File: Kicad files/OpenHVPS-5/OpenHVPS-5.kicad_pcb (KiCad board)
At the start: 2 copper layers, 40.6 x 20.8 mm, 80 parts, among them J1 Conn_01x03_Male, Q1 FQT7N10, Q2 BC846A, Q3 MMDT3906, U1 MAX6008AEUR+T, U2 74HC14, U3 MAX4162, U4 CD14538BM

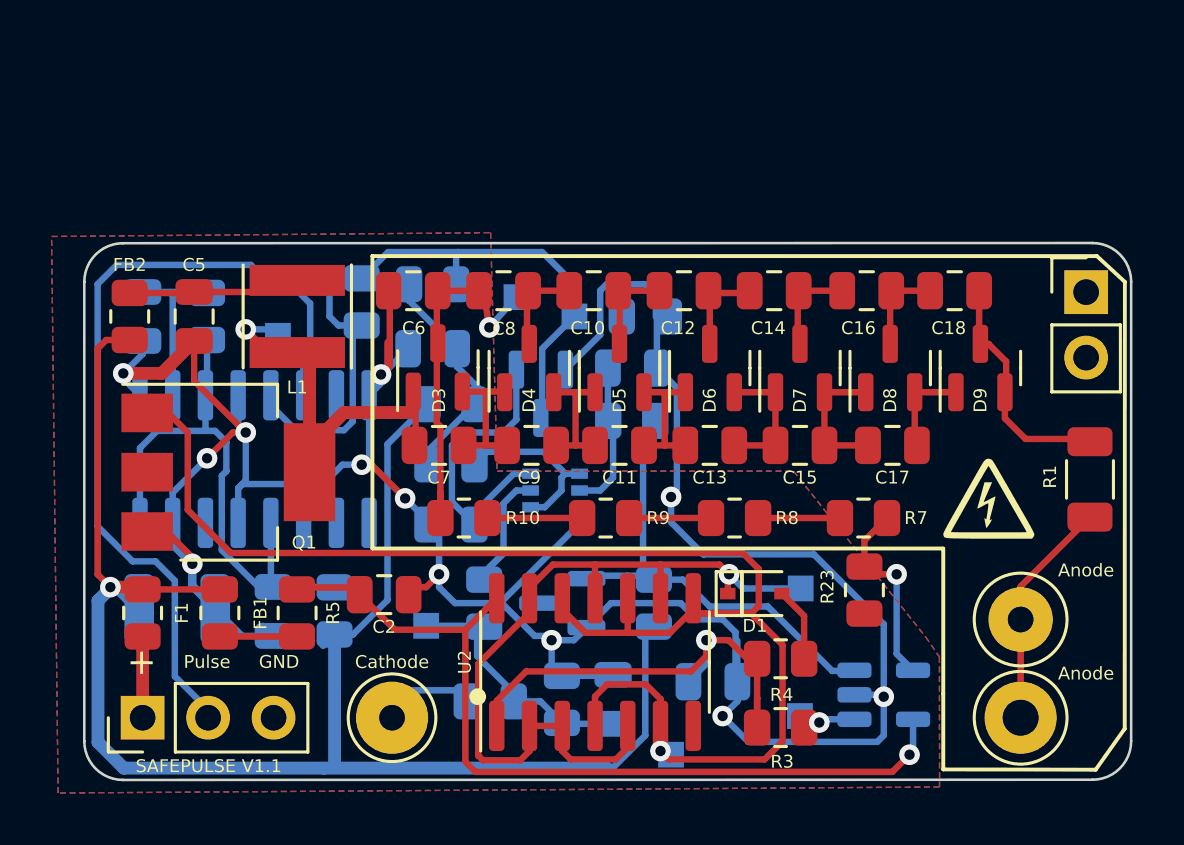
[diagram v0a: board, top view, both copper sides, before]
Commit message: Changed Q3 package to single transitor. Now Q3+Q4
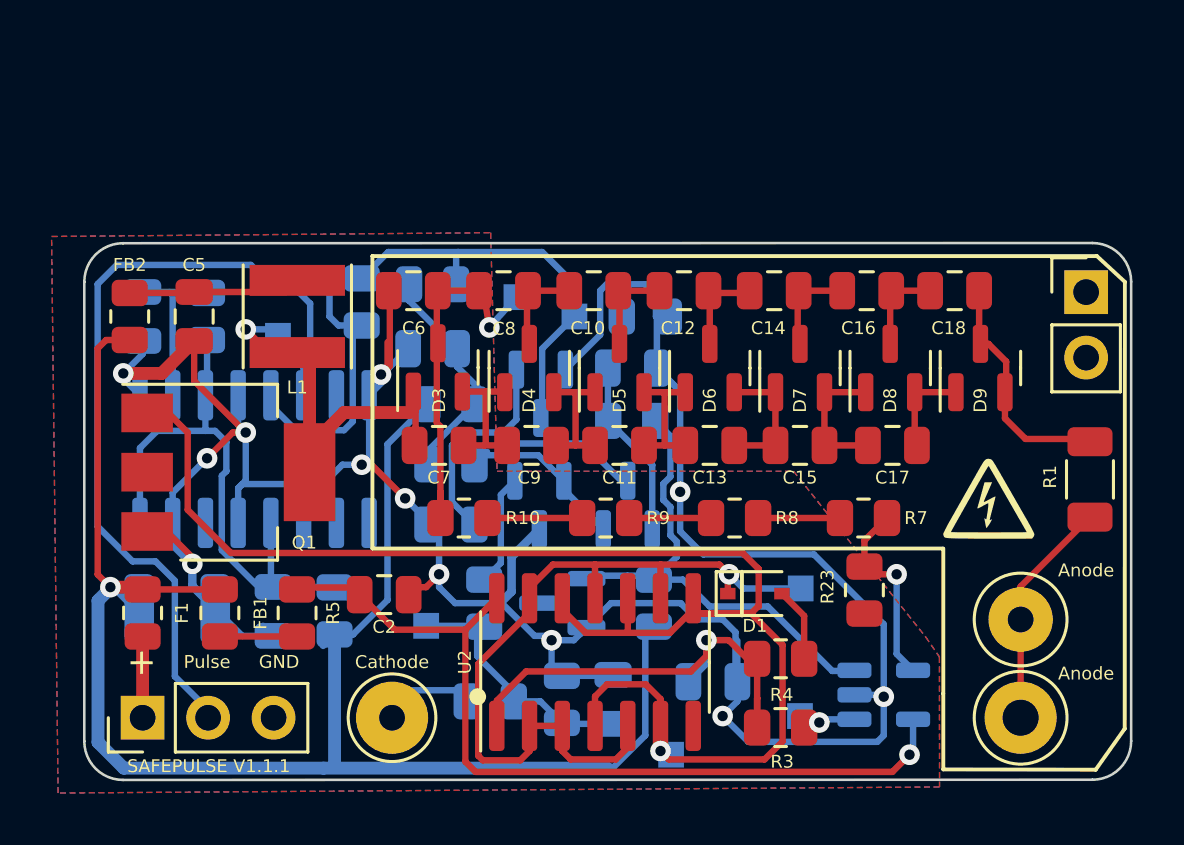
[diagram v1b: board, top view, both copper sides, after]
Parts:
- removed TP1: TestPoint, TestPoint:TestPoint_Pad_1.0x1.0mm
- added Q4: MMBT3906, Package_TO_SOT_SMD:SOT-23, B.Cu at (143.9, 67.3)
- Q3: value MMDT3906 -> MMBT3906; footprint Package_TO_SOT_SMD:SOT-363_SC-70-6 -> Package_TO_SOT_SMD:SOT-23
- moved Q3 2.88 mm to (147.3, 67.3), turned to 90 degrees
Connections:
- Q3 pad 1: Net-(Q3-Pad1) -> Net-(C24-Pad1)
- Q3 pad 2: Net-(C24-Pad1) -> Net-(R17-Pad2)
- Q3 pad 3: GND -> Net-(Q2-Pad1)
- R17 pad 2: Net-(Q3-Pad1) -> Net-(R17-Pad2)
- R19 pad 1: Net-(Q3-Pad5) -> Net-(R19-Pad1)
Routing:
- net Net-(R17-Pad2): track 0.00 -> 7.22 mm
- net Net-(Q3-Pad1): track 6.81 -> 0.00 mm
- net Net-(Q3-Pad5): track 5.39 -> 0.00 mm
- net Net-(R19-Pad1): track 0.00 -> 4.33 mm
- net Net-(Q2-Pad1): track 12.4 -> 15.0 mm
- net +2V5: track 18.9 -> 20.3 mm
- net Net-(C24-Pad1): track 8.12 -> 9.50 mm
- net GND: track 126.5 -> 125.9 mm
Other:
- board text added: "SAFEPULSE V1.1.1"
- board text removed: "SAFEPULSE V1.1"

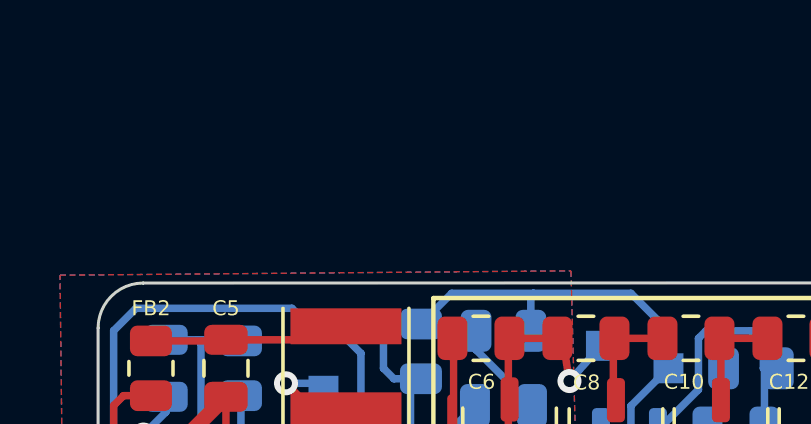
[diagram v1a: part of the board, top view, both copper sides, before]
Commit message: Removed TP1
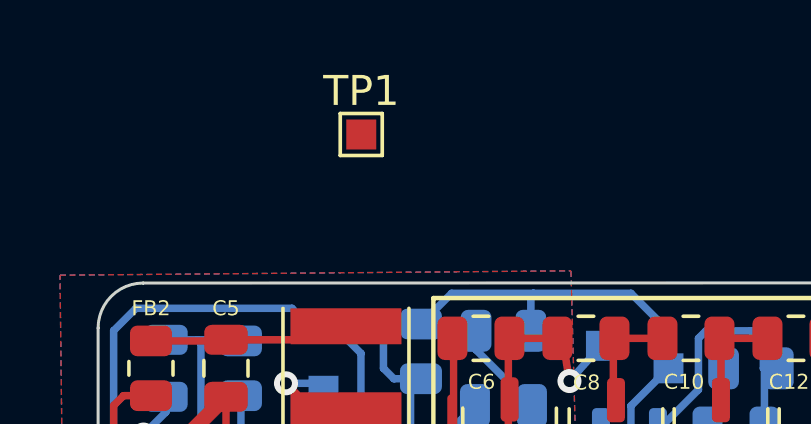
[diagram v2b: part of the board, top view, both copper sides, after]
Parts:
- added TP1: TestPoint, TestPoint:TestPoint_Pad_1.0x1.0mm, F.Cu at (135.0, 52.2)
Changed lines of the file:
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@@
   (net 47 "unconnected-(two_pinheader1-Pad2)")
   (net 48 "unconnected-(two_pinheader1-Pad1)")
-  (net 49 "Net-(R17-Pad2)")
-  (net 50 "Net-(R19-Pad1)")
+  (net 49 "Net-(Q3-Pad2)")
+  (net 50 "Net-(Q4-Pad1)")
   (footprint "Resistor_SMD:R_0805_2012Metric" (layer "F.Cu")
     (at 128.5 71.501 90)
@@
     )
   )
+  (footprint "TestPoint:TestPoint_Pad_1.0x1.0mm" (layer "F.Cu")
+    (at 135.01 52.206)
+    (descr "SMD rectangular pad as test Point, square 1.0mm side length")
+    (tags "test point SMD pad rectangle square")
+    (property "Sheetfile" "OpenHVPS-5.kicad_sch")
+    (property "Sheetname" "")
+    (property "exclude_from_bom" "")
+    (attr exclude_from_pos_files exclude_from_bom)
+    (fp_text reference "TP1" (at 0 -1.448) (layer "F.SilkS")
+      (effects (font (size 1 1) (thickness 0.15)))
+    )
+    (fp_text value "TestPoint" (at 0 1.55) (layer "F.Fab")
+      (effects (font (size 1 1) (thickness 0.15)))
+    )
+    (fp_text user "${REFERENCE}" (at 0 -1.45) (layer "F.Fab")
+      (effects (font (size 1 1) (thickness 0.15)))
+    )
+    (fp_line (start -0.7 -0.7) (end 0.7 -0.7) (layer "F.SilkS") (width 0.12))
+    (fp_line (start 0.7 0.7) (end -0.7 0.7) (layer "F.SilkS") (width 0.12))
+    (fp_line (start 0.7 -0.7) (end 0.7 0.7) (layer "F.SilkS") (width 0.12))
+    (fp_line (start -0.7 0.7) (end -0.7 -0.7) (layer "F.SilkS") (width 0.12))
+    (fp_line (start -1 -1) (end -1 1) (layer "F.CrtYd") (width 0.05))
+    (fp_line (start 1 1) (end 1 -1) (layer "F.CrtYd") (width 0.05))
+    (fp_line (start -1 -1) (end 1 -1) (layer "F.CrtYd") (width 0.05))
+    (fp_line (start 1 1) (end -1 1) (layer "F.CrtYd") (width 0.05))
+    (pad "1" smd rect (at 0 0) (locked) (size 1 1) (layers "F.Cu" "F.Mask")
+      (net 24 "+2V5") (pinfunction "1"))
+  )
   (footprint "Package_TO_SOT_SMD:SOT-23" (layer "F.Cu")
     (at 139.954 61.976 90)
@@
       (net 8 "Net-(C24-Pad1)") (pinfunction "B") (pintype "input"))
     (pad "2" smd roundrect (at -0.9375 -0.95 90) (locked) (size 1.475 0.6) (layers "B.Cu" "B.Paste" "B.Mask") (roundrect_rratio 0.25)
-      (net 49 "Net-(R17-Pad2)") (pinfunction "E") (pintype "passive"))
+      (net 49 "Net-(Q3-Pad2)") (pinfunction "E") (pintype "passive"))
     (pad "3" smd roundrect (at 0.9375 0 90) (locked) (size 1.475 0.6) (layers "B.Cu" "B.Paste" "B.Mask") (roundrect_rratio 0.25)
       (net 20 "Net-(Q2-Pad1)") (pinfunction "C") (pintype "passive"))
@@
       (net 35 "Net-(C19-Pad1)") (pintype "passive"))
     (pad "2" smd roundrect (at 0.9125 0) (locked) (size 1.025 1.4) (layers "B.Cu" "B.Paste" "B.Mask") (roundrect_rratio 0.243902)
-      (net 49 "Net-(R17-Pad2)") (pintype "passive"))
+      (net 49 "Net-(Q3-Pad2)") (pintype "passive"))
     (model "${KICAD6_3DMODEL_DIR}/Resistor_SMD.3dshapes/R_0805_2012Metric.wrl"
       (offset (xyz 0 0 0))
@@
     (fp_line (start -0.65 1.125) (end -0.325 1.45) (layer "B.Fab") (width 0.1))
     (pad "1" smd roundrect (at -0.9375 0.95 270) (locked) (size 1.475 0.6) (layers "B.Cu" "B.Paste" "B.Mask") (roundrect_rratio 0.25)
-      (net 50 "Net-(R19-Pad1)") (pinfunction "B") (pintype "input"))
+      (net 50 "Net-(Q4-Pad1)") (pinfunction "B") (pintype "input"))
     (pad "2" smd roundrect (at -0.9375 -0.95 270) (locked) (size 1.475 0.6) (layers "B.Cu" "B.Paste" "B.Mask") (roundrect_rratio 0.25)
-      (net 49 "Net-(R17-Pad2)") (pinfunction "E") (pintype "passive"))
+      (net 49 "Net-(Q3-Pad2)") (pinfunction "E") (pintype "passive"))
     (pad "3" smd roundrect (at 0.9375 0 270) (locked) (size 1.475 0.6) (layers "B.Cu" "B.Paste" "B.Mask") (roundrect_rratio 0.25)
       (net 3 "GND") (pinfunction "C") (pintype "passive"))
@@
     (fp_line (start 1 -0.625) (end -1 -0.625) (layer "B.Fab") (width 0.1))
     (pad "1" smd roundrect (at -0.9125 0 270) (locked) (size 1.025 1.4) (layers "B.Cu" "B.Paste" "B.Mask") (roundrect_rratio 0.243902)
-      (net 50 "Net-(R19-Pad1)") (pintype "passive"))
+      (net 50 "Net-(Q4-Pad1)") (pintype "passive"))
     (pad "2" smd roundrect (at 0.9125 0 270) (locked) (size 1.025 1.4) (layers "B.Cu" "B.Paste" "B.Mask") (roundrect_rratio 0.243902)
       (net 28 "Net-(C22-Pad1)") (pintype "passive"))

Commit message: Removed TP1 from PCB
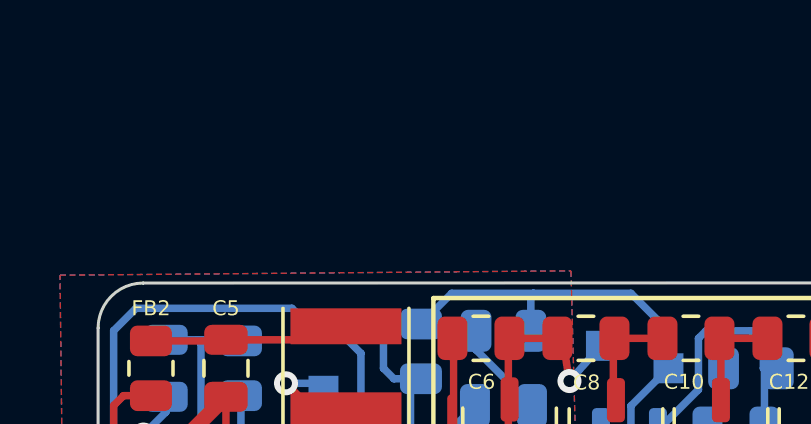
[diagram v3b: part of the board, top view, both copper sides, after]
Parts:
- removed TP1: TestPoint, TestPoint:TestPoint_Pad_1.0x1.0mm
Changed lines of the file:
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@@
     )
-  )
-  (footprint "TestPoint:TestPoint_Pad_1.0x1.0mm" (layer "F.Cu")
-    (at 135.01 52.206)
-    (descr "SMD rectangular pad as test Point, square 1.0mm side length")
-    (tags "test point SMD pad rectangle square")
-    (property "Sheetfile" "OpenHVPS-5.kicad_sch")
-    (property "Sheetname" "")
-    (property "exclude_from_bom" "")
-    (attr exclude_from_pos_files exclude_from_bom)
-    (fp_text reference "TP1" (at 0 -1.448) (layer "F.SilkS")
-      (effects (font (size 1 1) (thickness 0.15)))
-    )
-    (fp_text value "TestPoint" (at 0 1.55) (layer "F.Fab")
-      (effects (font (size 1 1) (thickness 0.15)))
-    )
-    (fp_text user "${REFERENCE}" (at 0 -1.45) (layer "F.Fab")
-      (effects (font (size 1 1) (thickness 0.15)))
-    )
-    (fp_line (start -0.7 -0.7) (end 0.7 -0.7) (layer "F.SilkS") (width 0.12))
-    (fp_line (start 0.7 0.7) (end -0.7 0.7) (layer "F.SilkS") (width 0.12))
-    (fp_line (start 0.7 -0.7) (end 0.7 0.7) (layer "F.SilkS") (width 0.12))
-    (fp_line (start -0.7 0.7) (end -0.7 -0.7) (layer "F.SilkS") (width 0.12))
-    (fp_line (start -1 -1) (end -1 1) (layer "F.CrtYd") (width 0.05))
-    (fp_line (start 1 1) (end 1 -1) (layer "F.CrtYd") (width 0.05))
-    (fp_line (start -1 -1) (end 1 -1) (layer "F.CrtYd") (width 0.05))
-    (fp_line (start 1 1) (end -1 1) (layer "F.CrtYd") (width 0.05))
-    (pad "1" smd rect (at 0 0) (locked) (size 1 1) (layers "F.Cu" "F.Mask")
-      (net 24 "+2V5") (pinfunction "1"))
   )
   (footprint "Package_TO_SOT_SMD:SOT-23" (layer "F.Cu")

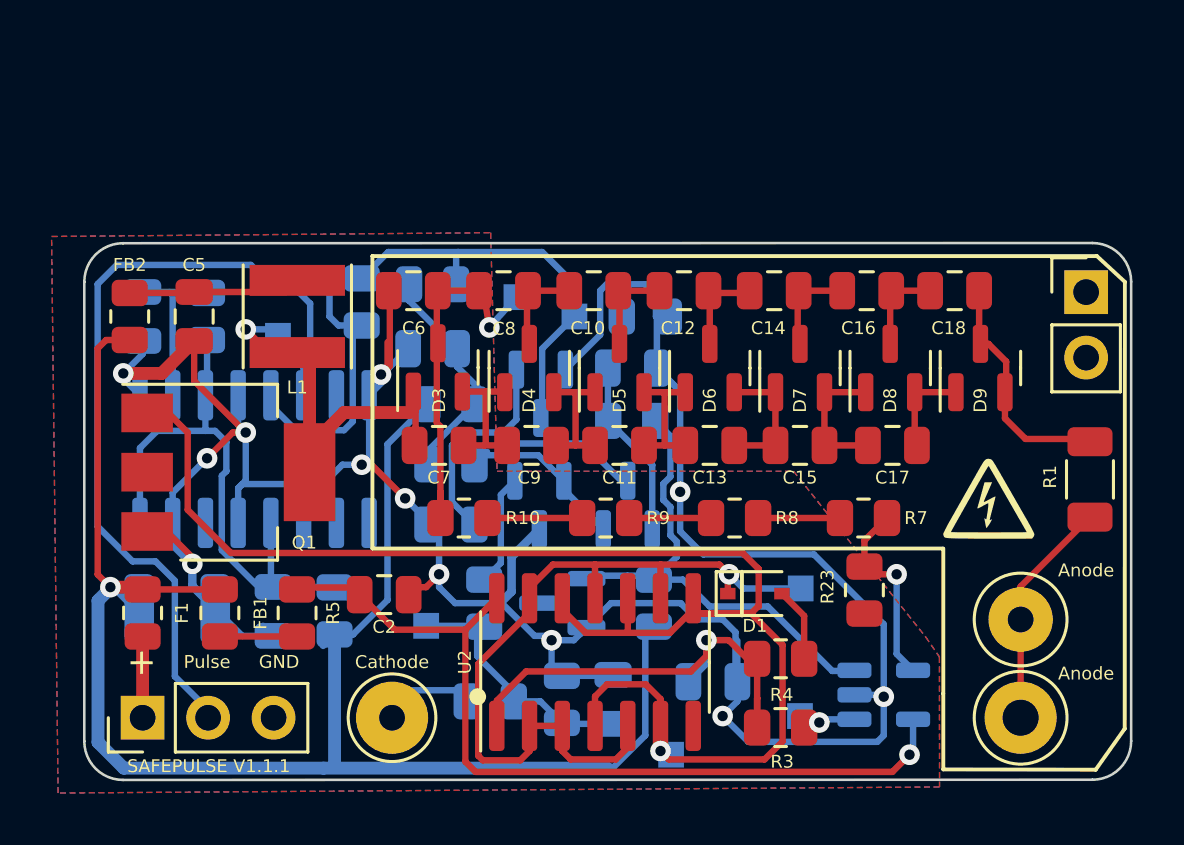
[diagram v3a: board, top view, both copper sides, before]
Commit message: Added cap for smoothing opamp
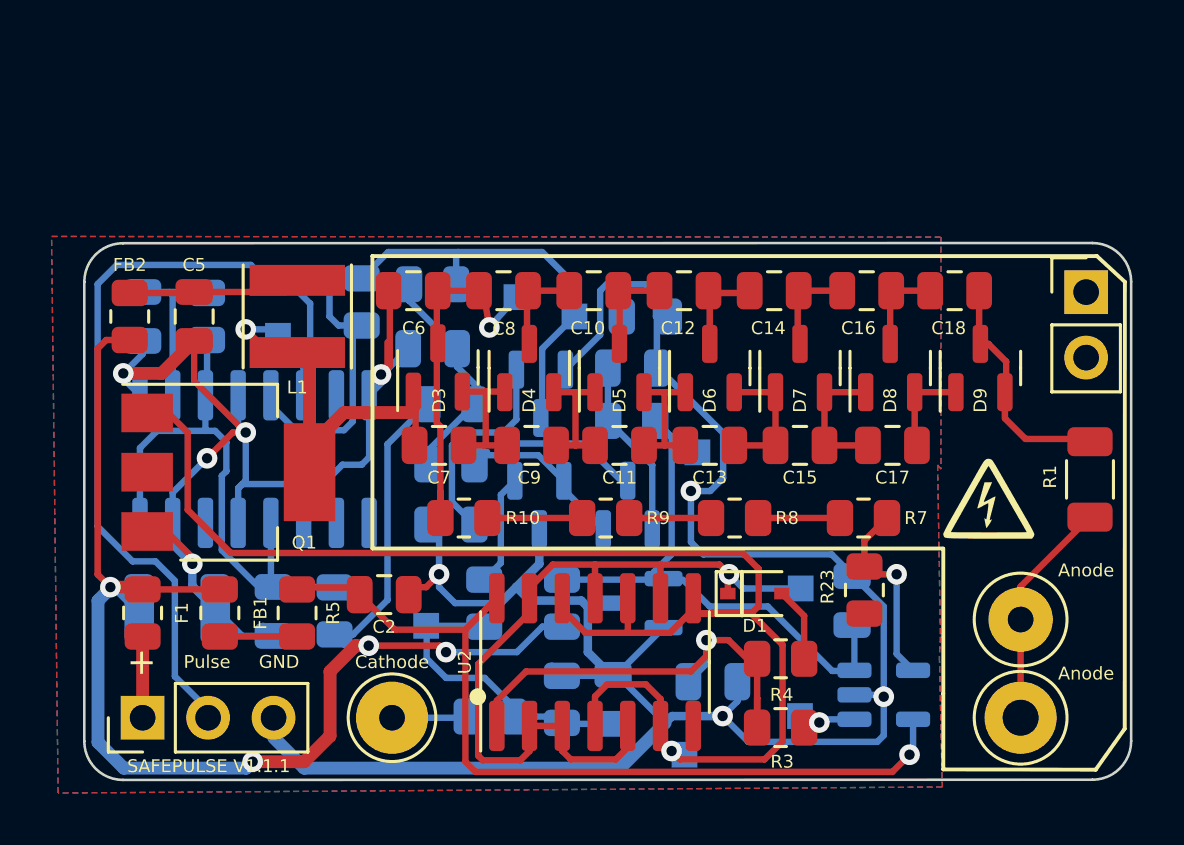
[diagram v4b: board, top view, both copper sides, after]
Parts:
- added C25: 1nF, Capacitor_SMD:C_0805_2012Metric, B.Cu at (156.0, 71.0)
- added TP1: TestPoint, TestPoint:TestPoint_Pad_1.0x1.0mm, B.Cu at (150.0, 65.3)
- moved R20 3.57 mm to (144.8, 71.1)
- moved U1 2.99 mm to (147.8, 71.1)
- moved R21 0.59 mm to (142.0, 75.5)
- moved TP4 0.52 mm to (149.5, 77.0)
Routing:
- net GND: track 125.9 -> 139.1 mm, vias 12 -> 9
- net +3V3: track 67.0 -> 58.6 mm, vias 1 -> 4
- net +2V5: track 20.3 -> 23.8 mm
- net Net-(C22-Pad1): track 9.74 -> 11.8 mm
